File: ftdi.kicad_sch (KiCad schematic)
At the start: 31 parts, among them U1301 AT93C56, U1302 FT2232HL, Y1301 12MHz CL=18p

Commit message: Schematic: add PNs for resistors
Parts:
- R1301: Mfr (none) -> Bourns; Mfr PN (none) -> CR0805-FX-5101ELF
- R1302, R1305, R1307, R1309, R1310, R1311: Mfr (none) -> Bourns; Mfr PN (none) -> CR0805-FX-1002ELF
- R1303, R1304: Mfr (none) -> Bourns; Mfr PN (none) -> CR0805-J/-000ELF
- R1306: Mfr (none) -> Bourns; Mfr PN (none) -> CR0805-FX-2401ELF
- R1308: Mfr (none) -> Bourns; Mfr PN (none) -> CR0805-FX-1202ELF
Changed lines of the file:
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@@
+      (effects (font (size 1.27 1.27)) hide)
+    )
+    (property "Mfr" "Bourns" (id 4) (at 57.15 81.28 0)
+      (effects (font (size 1.27 1.27)) hide)
+    )
+    (property "Mfr PN" "CR0805-J/-000ELF" (id 5) (at 57.15 81.28 0)
       (effects (font (size 1.27 1.27)) hide)
     )
@@
       (effects (font (size 1.27 1.27)) hide)
     )
+    (property "Mfr" "Bourns" (id 5) (at 38.1 158.75 0)
+      (effects (font (size 1.27 1.27)) hide)
+    )
+    (property "Mfr PN" "CR0805-FX-5101ELF" (id 6) (at 38.1 158.75 0)
+      (effects (font (size 1.27 1.27)) hide)
+    )
     (pin "1")
     (pin "2")
@@
     )
     (property "Tolerance" "" (id 4) (at 38.1 171.45 0)
+      (effects (font (size 1.27 1.27)) hide)
+    )
+    (property "Mfr" "Bourns" (id 5) (at 38.1 171.45 0)
+      (effects (font (size 1.27 1.27)) hide)
+    )
+    (property "Mfr PN" "CR0805-FX-1002ELF" (id 6) (at 38.1 171.45 0)
       (effects (font (size 1.27 1.27)) hide)
     )
@@
       (effects (font (size 1.27 1.27)) hide)
     )
+    (property "Mfr" "Bourns" (id 4) (at 57.15 76.2 0)
+      (effects (font (size 1.27 1.27)) hide)
+    )
+    (property "Mfr PN" "CR0805-J/-000ELF" (id 5) (at 57.15 76.2 0)
+      (effects (font (size 1.27 1.27)) hide)
+    )
     (pin "1")
     (pin "2")
@@
       (effects (font (size 1.27 1.27)) hide)
     )
+    (property "Mfr" "Bourns" (id 5) (at 83.82 123.19 0)
+      (effects (font (size 1.27 1.27)) hide)
+    )
+    (property "Mfr PN" "CR0805-FX-2401ELF" (id 6) (at 83.82 123.19 0)
+      (effects (font (size 1.27 1.27)) hide)
+    )
     (pin "1")
     (pin "2")
@@
       (effects (font (size 1.27 1.27)) hide)
     )
+    (property "Mfr" "Bourns" (id 5) (at 86.36 101.6 0)
+      (effects (font (size 1.27 1.27)) hide)
+    )
+    (property "Mfr PN" "CR0805-FX-1002ELF" (id 6) (at 86.36 101.6 0)
+      (effects (font (size 1.27 1.27)) hide)
+    )
     (pin "1")
     (pin "2")
@@
     )
     (property "Tolerance" "" (id 4) (at 96.52 101.6 0)
+      (effects (font (size 1.27 1.27)) hide)
+    )
+    (property "Mfr" "Bourns" (id 5) (at 96.52 101.6 0)
+      (effects (font (size 1.27 1.27)) hide)
+    )
+    (property "Mfr PN" "CR0805-FX-1002ELF" (id 6) (at 96.52 101.6 0)
       (effects (font (size 1.27 1.27)) hide)
     )
@@
       (effects (font (size 1.27 1.27)) hide)
     )
+    (property "Mfr" "Bourns" (id 5) (at 102.87 96.52 0)
+      (effects (font (size 1.27 1.27)) hide)
+    )
+    (property "Mfr PN" "CR0805-FX-1002ELF" (id 6) (at 102.87 96.52 0)
+      (effects (font (size 1.27 1.27)) hide)
+    )
     (pin "1")
     (pin "2")
@@
     )
     (property "Tolerance" "" (id 4) (at 95.25 85.09 0)
+      (effects (font (size 1.27 1.27)) hide)
+    )
+    (property "Mfr" "Bourns" (id 5) (at 95.25 85.09 0)
+      (effects (font (size 1.27 1.27)) hide)
+    )
+    (property "Mfr PN" "CR0805-FX-1202ELF" (id 6) (at 95.25 85.09 0)
       (effects (font (size 1.27 1.27)) hide)
     )
@@
       (effects (font (size 1.27 1.27)) hide)
     )
+    (property "Mfr" "Bourns" (id 5) (at 76.2 101.6 0)
+      (effects (font (size 1.27 1.27)) hide)
+    )
+    (property "Mfr PN" "CR0805-FX-1002ELF" (id 6) (at 76.2 101.6 0)
+      (effects (font (size 1.27 1.27)) hide)
+    )
     (pin "1")
     (pin "2")
@@
       (effects (font (size 1.27 1.27)) hide)
     )
+    (property "Mfr" "Bourns" (id 5) (at 177.8 125.73 0)
+      (effects (font (size 1.27 1.27)) hide)
+    )
+    (property "Mfr PN" "CR0805-FX-1002ELF" (id 6) (at 177.8 125.73 0)
+      (effects (font (size 1.27 1.27)) hide)
+    )

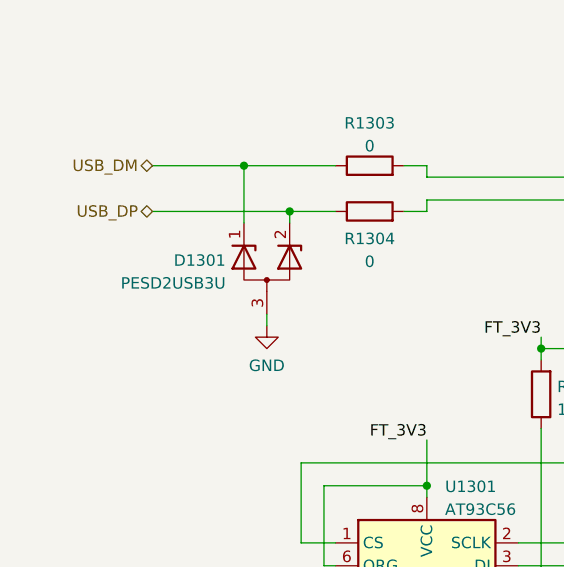
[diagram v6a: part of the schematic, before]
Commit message: Update footprints: - SOD323F, SOD323, SOD123W... intead of generic handsolder version - 3225 xtal - use handsolder footprint - do not use handsolder version for ferrite beads - use SOT-23-6 instead of TSOP-6
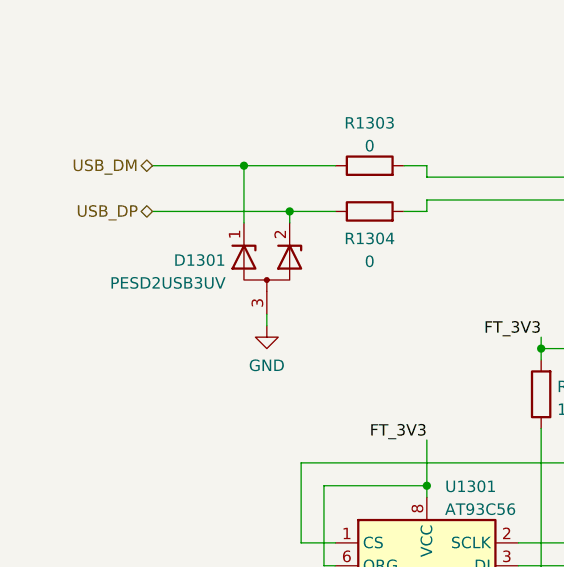
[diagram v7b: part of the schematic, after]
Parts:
- D1301: value PESD2USB3U -> PESD2USB3UV
- FB1301, FB1302: footprint Inductor_SMD:L_0805_2012Metric_Pad1.05x1.20mm_HandSolder -> Inductor_SMD:L_0805_2012Metric
- Y1301: footprint Crystal:Crystal_SMD_3225-4Pin_3.2x2.5mm -> Crystal:Crystal_SMD_3225-4Pin_3.2x2.5mm_HandSoldering
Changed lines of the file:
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@@
     (property "Reference" "FB1302" (id 0) (at 247.7008 95.2586 90))
     (property "Value" "782853701" (id 1) (at 247.7008 97.7955 90))
-    (property "Footprint" "Inductor_SMD:L_0805_2012Metric_Pad1.05x1.20mm_HandSolder" (id 2) (at 247.65 99.822 90)
+    (property "Footprint" "Inductor_SMD:L_0805_2012Metric" (id 2) (at 247.65 99.822 90)
       (effects (font (size 1.27 1.27)) hide)
     )
@@
     (property "Reference" "FB1301" (id 0) (at 247.7008 63.5086 90))
     (property "Value" "782853701" (id 1) (at 247.7008 66.0455 90))
-    (property "Footprint" "Inductor_SMD:L_0805_2012Metric_Pad1.05x1.20mm_HandSolder" (id 2) (at 247.65 68.072 90)
+    (property "Footprint" "Inductor_SMD:L_0805_2012Metric" (id 2) (at 247.65 68.072 90)
       (effects (font (size 1.27 1.27)) hide)
     )
@@
       (effects (font (size 1.27 1.27)) (justify left))
     )
-    (property "Footprint" "Crystal:Crystal_SMD_3225-4Pin_3.2x2.5mm" (id 2) (at 87.63 140.97 0)
+    (property "Footprint" "Crystal:Crystal_SMD_3225-4Pin_3.2x2.5mm_HandSoldering" (id 2) (at 87.63 140.97 0)
       (effects (font (size 1.27 1.27)) hide)
     )
@@
       (effects (font (size 1.27 1.27)) (justify left))
     )
-    (property "Value" "PESD2USB3U" (id 1) (at 41.1481 89.2687 90)
-      (effects (font (size 1.27 1.27)) (justify left))
-    )
+    (property "Value" "PESD2USB3UV" (id 1) (at 41.1481 89.2687 90)
+      (effects (font (size 1.27 1.27)) (justify left))
+    )

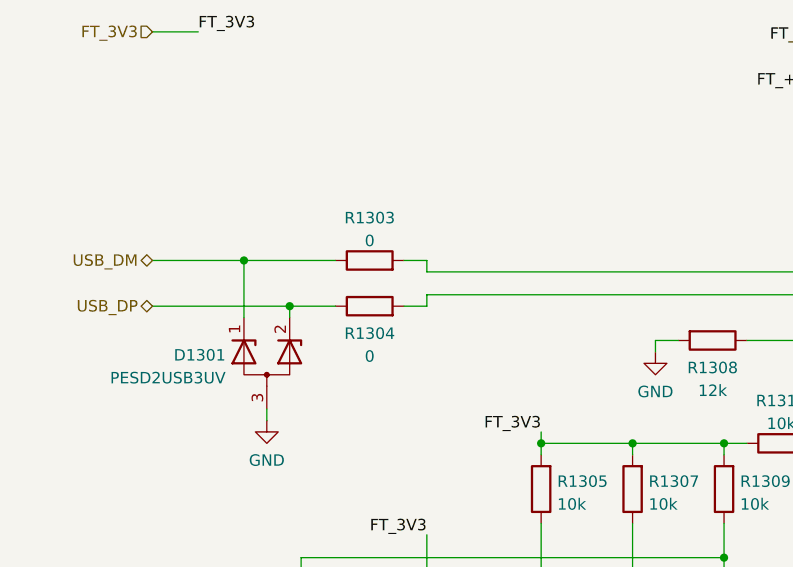
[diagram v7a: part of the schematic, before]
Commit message: Rename USB dp,dm to d+,d- to make pcbnew happy
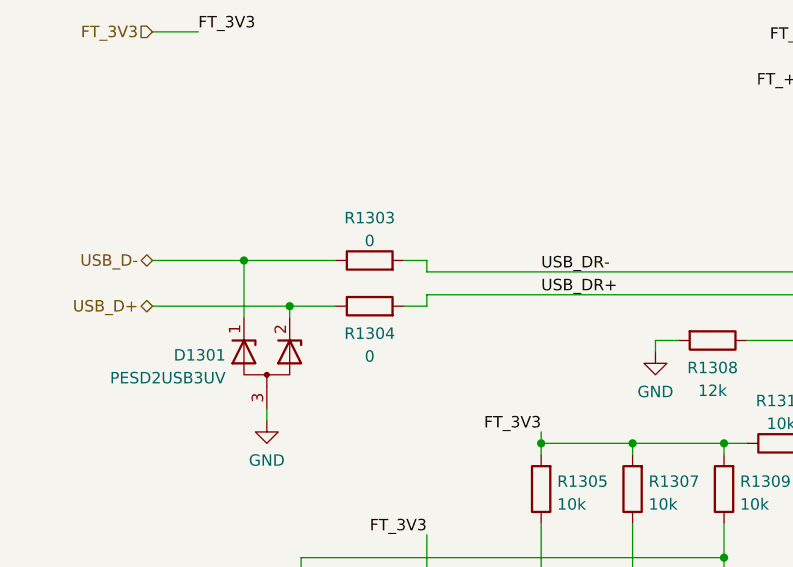
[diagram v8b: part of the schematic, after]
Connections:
- net USB_DR+: now reaches R1304.2, U1302.8 (DP)
- net USB_DR-: now reaches R1303.2, U1302.7 (DM)
- net USB_DM renamed USB_D-
- net USB_DP renamed USB_D+
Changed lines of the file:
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@@
     (effects (font (size 1.27 1.27)) (justify right bottom))
+  )
+  (label "USB_DR-" (at 76.2 77.47 0)
+    (effects (font (size 1.27 1.27)) (justify left bottom))
   )
   (label "FT_+3V3" (at 184.15 125.73 0)
@@
   (label "IOB.IO1" (at 210.82 113.03 180)
     (effects (font (size 1.27 1.27)) (justify right bottom))
+  )
+  (label "USB_DR+" (at 76.2 80.01 0)
+    (effects (font (size 1.27 1.27)) (justify left bottom))
   )
   (label "FIFO.D5" (at 187.96 64.77 180)
@@
     (effects (font (size 1.27 1.27)) (justify left))
   )
-  (hierarchical_label "USB_DP" (shape bidirectional) (at 33.02 81.28 180)
+  (hierarchical_label "USB_D+" (shape bidirectional) (at 33.02 81.28 180)
     (effects (font (size 1.27 1.27)) (justify right))
   )
@@
     (effects (font (size 1.27 1.27)) (justify right))
   )
-  (hierarchical_label "USB_DM" (shape bidirectional) (at 33.02 76.2 180)
+  (hierarchical_label "USB_D-" (shape bidirectional) (at 33.02 76.2 180)
     (effects (font (size 1.27 1.27)) (justify right))
   )
